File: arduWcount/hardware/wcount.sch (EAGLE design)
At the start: 25 parts, among them IC1 MEGA8-AI, Q2 BC447, Q4 BC447

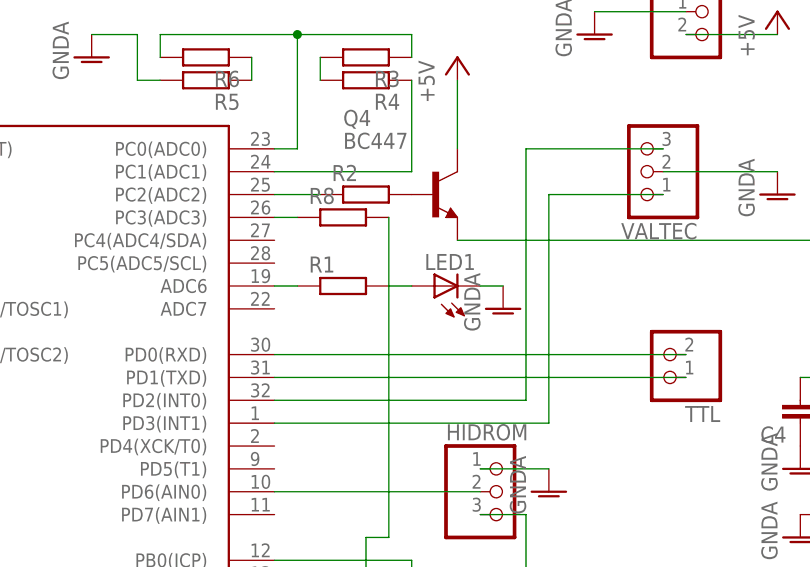
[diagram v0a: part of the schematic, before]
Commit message: EEPROM rotating added
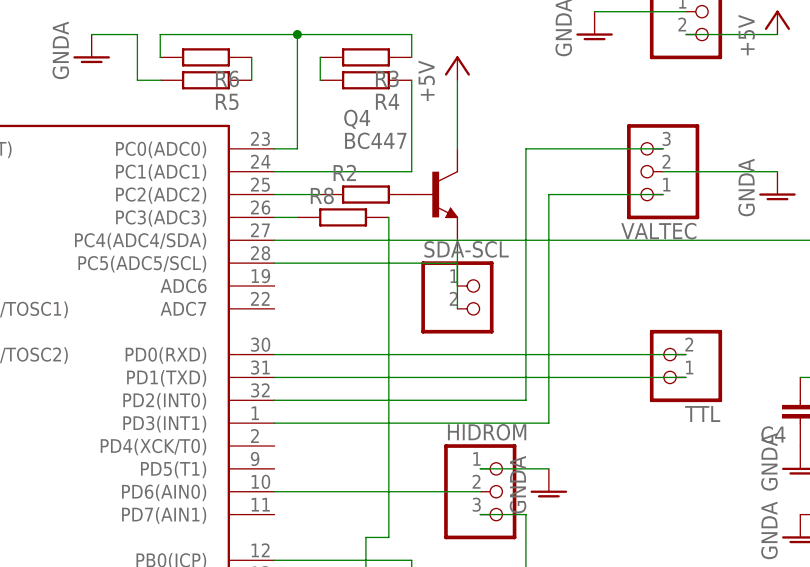
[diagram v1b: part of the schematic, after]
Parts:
- removed LED1: (no value), led:LED3MM
- removed R1: (no value), resistor:R-EU_R0805
- added SDA-SCL: (no value), pinhead:PINHD-1X2
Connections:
- net GNDA: no longer LED1.C
- net N$22: now also IC1.PC4(ADC4/SDA), SDA-SCL.1; no longer LED1.A, R1.2
- net N$23: now also IC1.PC5(ADC5/SCL), SDA-SCL.2; no longer IC1.ADC6, R1.1
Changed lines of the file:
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@@
 <part name="C3" library="eagle-ltspice" deviceset="C" device=""/>
 <part name="C4" library="eagle-ltspice" deviceset="C" device=""/>
-<part name="LED1" library="led" deviceset="LED" device="3MM"/>
-<part name="R1" library="resistor" deviceset="R-EU_" device="R0805"/>
 <part name="R5" library="resistor" deviceset="R-EU_" device="R0805"/>
 <part name="R6" library="resistor" deviceset="R-EU_" device="R0805"/>
@@
 <part name="Q2" library="transistor-npn" deviceset="BC447*" device=""/>
 <part name="GND1" library="supply1" deviceset="GNDA" device=""/>
-<part name="GND2" library="supply1" deviceset="GNDA" device=""/>
 <part name="GND6" library="supply1" deviceset="GNDA" device=""/>
 <part name="GND8" library="supply1" deviceset="GNDA" device=""/>
@@
 <part name="SV1" library="con-lsta" deviceset="FE05-2" device=""/>
 <part name="C5" library="resistor" deviceset="C-EU" device="C0805" value="0.1 mf"/>
+<part name="SDA-SCL" library="pinhead" deviceset="PINHD-1X2" device=""/>
 </parts>
 <sheets>
@@
 <instance part="C3" gate="G$1" x="132.08" y="27.94" rot="R180"/>
 <instance part="C4" gate="G$1" x="121.92" y="58.42" rot="R180"/>
-<instance part="LED1" gate="G$1" x="81.28" y="73.66" rot="R90"/>
-<instance part="R1" gate="G$1" x="71.12" y="73.66"/>
 <instance part="R5" gate="G$1" x="55.88" y="96.52" rot="R180"/>
 <instance part="R6" gate="G$1" x="55.88" y="99.06" rot="R180"/>
@@
 <instance part="Q2" gate="G$1" x="119.38" y="27.94" rot="R270"/>
 <instance part="GND1" gate="1" x="58.42" y="2.54"/>
-<instance part="GND2" gate="1" x="88.9" y="71.12"/>
 <instance part="GND6" gate="1" x="43.18" y="99.06"/>
 <instance part="GND8" gate="1" x="0" y="91.44"/>
@@
 <instance part="SV1" gate="G$1" x="88.9" y="17.78" rot="R270"/>
 <instance part="C5" gate="G$1" x="43.18" y="22.86"/>
+<instance part="SDA-SCL" gate="G$1" x="86.36" y="71.12"/>
 </instances>
 <busses>
@@
 </segment>
 </net>
-<net name="N$22" class="0">
-<segment>
-<pinref part="LED1" gate="G$1" pin="A"/>
-<pinref part="R1" gate="G$1" pin="2"/>
-<wire x1="78.74" y1="73.66" x2="76.2" y2="73.66" width="0.1524" layer="91"/>
-</segment>
-</net>
-<net name="N$23" class="0">
-<segment>
-<pinref part="IC1" gate="G$1" pin="ADC6"/>
-<pinref part="R1" gate="G$1" pin="1"/>
-<wire x1="63.5" y1="73.66" x2="66.04" y2="73.66" width="0.1524" layer="91"/>
-</segment>
-</net>
 <net name="N$25" class="0">
 <segment>
@@
 <wire x1="48.26" y1="101.6" x2="43.18" y2="101.6" width="0.1524" layer="91"/>
 <pinref part="GND6" gate="1" pin="GNDA"/>
-</segment>
-<segment>
-<pinref part="LED1" gate="G$1" pin="C"/>
-<wire x1="86.36" y1="73.66" x2="88.9" y2="73.66" width="0.1524" layer="91"/>
-<pinref part="GND2" gate="1" pin="GNDA"/>
 </segment>
 <segment>
@@
 </segment>
 </net>
+<net name="N$22" class="0">
+<segment>
+<pinref part="IC1" gate="G$1" pin="PC4(ADC4/SDA)"/>
+<pinref part="SDA-SCL" gate="G$1" pin="1"/>
+<wire x1="63.5" y1="78.74" x2="83.82" y2="78.74" width="0.1524" layer="91"/>
+<wire x1="83.82" y1="78.74" x2="83.82" y2="73.66" width="0.1524" layer="91"/>
+</segment>
+</net>
+<net name="N$23" class="0">
+<segment>
+<pinref part="IC1" gate="G$1" pin="PC5(ADC5/SCL)"/>
+<pinref part="SDA-SCL" gate="G$1" pin="2"/>
+<wire x1="63.5" y1="76.2" x2="83.82" y2="76.2" width="0.1524" layer="91"/>
+<wire x1="83.82" y1="76.2" x2="83.82" y2="71.12" width="0.1524" layer="91"/>
+</segment>
+</net>
